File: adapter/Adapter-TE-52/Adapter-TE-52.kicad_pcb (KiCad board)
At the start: 2 copper layers, 75 x 45.1 mm, 2 parts, among them U1 Adapter-TE-52, U2 TE-AUTO-CONN-52

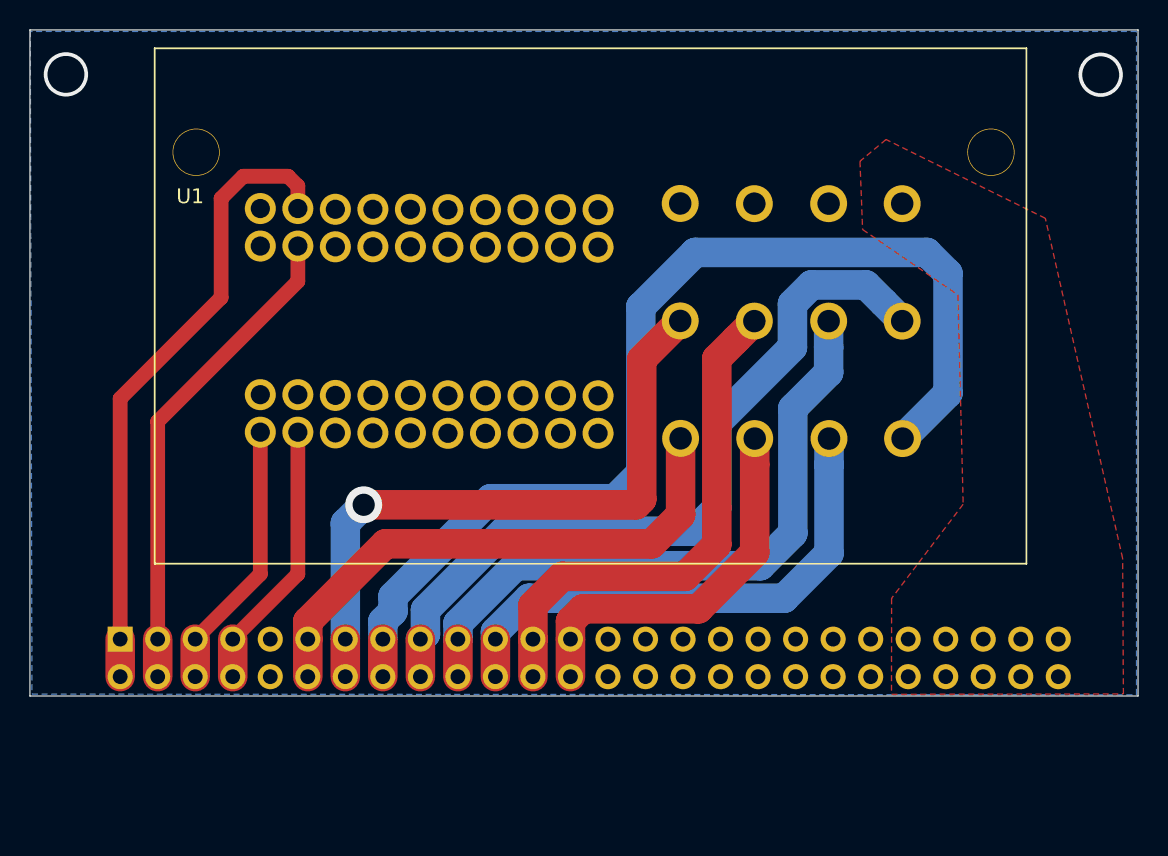
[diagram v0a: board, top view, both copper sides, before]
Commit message: modified adapter, TE 52
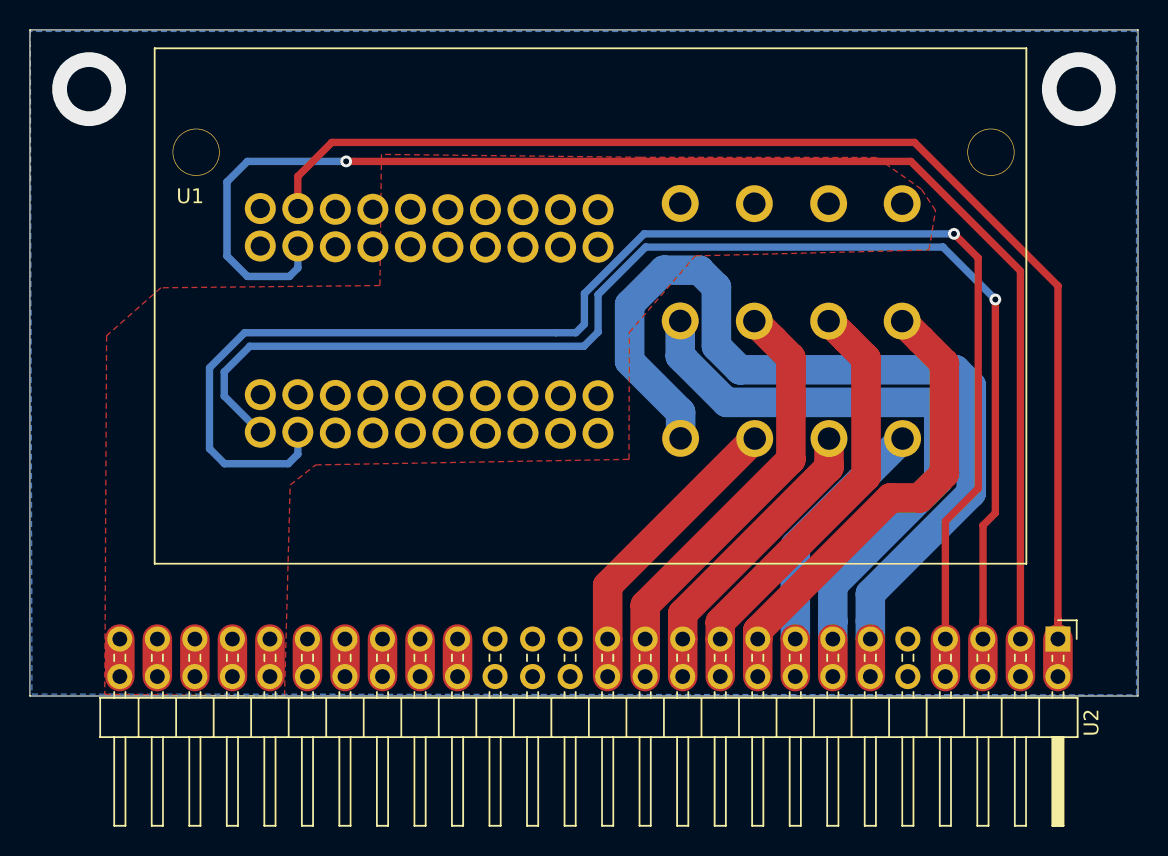
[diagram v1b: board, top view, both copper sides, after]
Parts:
- added LOGO: , open-automation:LOGO, B.Cu at (140.1, 81.1)
- U2: moved to F.Cu
- moved U2 7.64 mm to (131.7, 124.4), turned to 0 degrees
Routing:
- net /CAMERA-: track 18.4 -> 100.6 mm, vias 0 -> 1
- net /CAMERA+: track 18.4 -> 89.6 mm, vias 0 -> 1
- net /CAN-: track 33.1 -> 96.9 mm, vias 0 -> 1
- net /LR-: track 72.6 -> 19.1 mm
- net /CAN+: track 42.8 -> 86.4 mm
- net /RR-: track 37.1 -> 62.7 mm
- net /LR+: track 52.2 -> 31.6 mm
- net /LF-: track 35.6 -> 20.2 mm
- net /LF+: track 44.2 -> 29.2 mm
- net GND: track 0.00 -> 12.7 mm, vias 0 -> 2
- net /BATTERY: track 0.00 -> 12.7 mm
- net /RF+: track 35.2 -> 29.2 mm
- net /RF-: track 25.9 -> 20.2 mm
- net /RR+: track 44.3 -> 42.7 mm, vias 1 -> 0
- net (no net): vias 2 -> 0
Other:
- board text added: "GND"
